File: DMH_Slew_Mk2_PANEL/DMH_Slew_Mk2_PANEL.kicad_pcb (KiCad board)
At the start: 2 copper layers, 50 x 200 mm, 27 parts

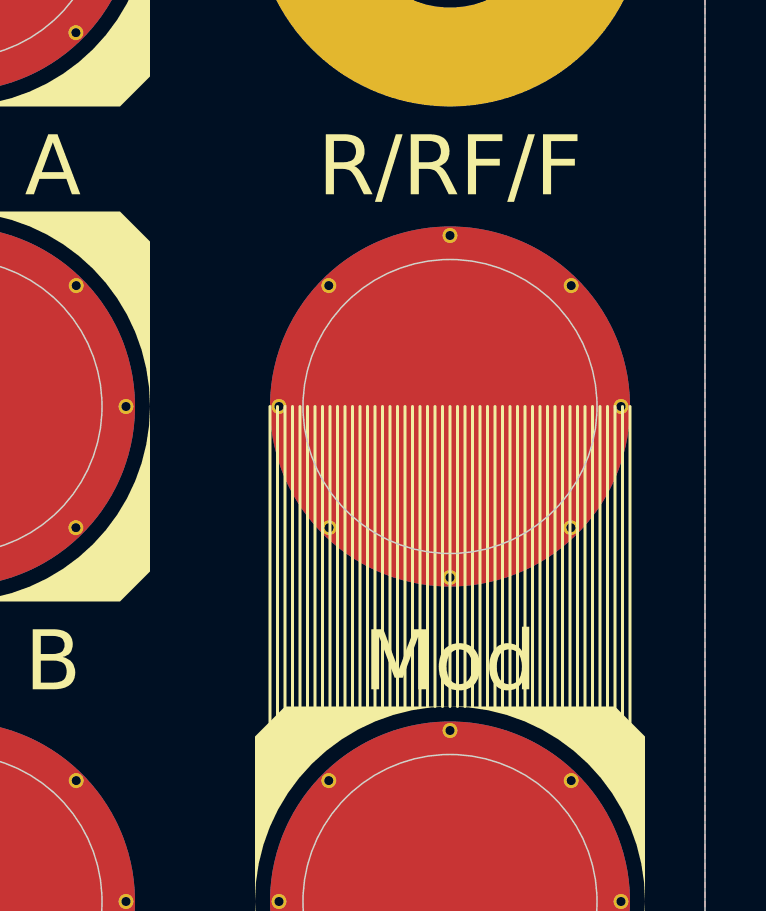
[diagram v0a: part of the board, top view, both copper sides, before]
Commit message: Designed Controls PCB
... and removed Mod feature
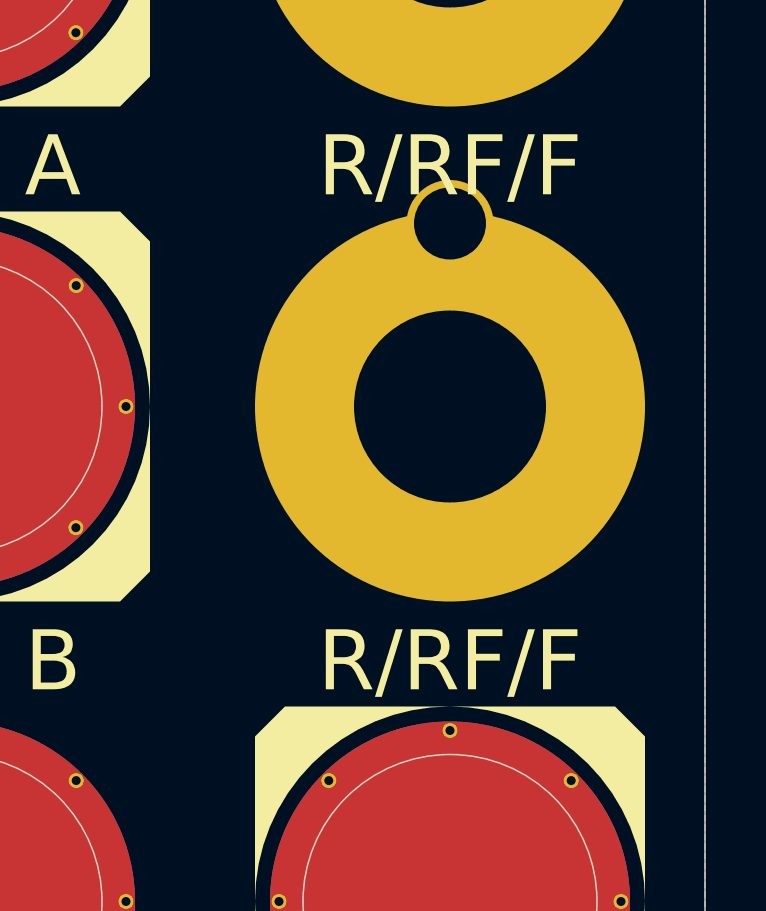
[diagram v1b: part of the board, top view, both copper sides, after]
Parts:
- H18: value Mod -> R/RF/F; footprint SynthStuff:Jack_6.35mm_Cutout_v3 -> SynthStuff:Toggle_Switch_TE_Cutout
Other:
- board text added: "Mk2.0 - April 2026"
- board text removed: "Mk1.0 - March 2026"
